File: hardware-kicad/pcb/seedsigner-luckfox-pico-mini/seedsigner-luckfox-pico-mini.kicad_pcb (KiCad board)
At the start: 2 copper layers, 100 x 100 mm, 37 parts, among them J1 Conn_01x10, J2 Conn_01x05, U1 LuckFox_Pico_PLUS_PRO, U2 RASPBERRY_PI_3_MODEL_B+

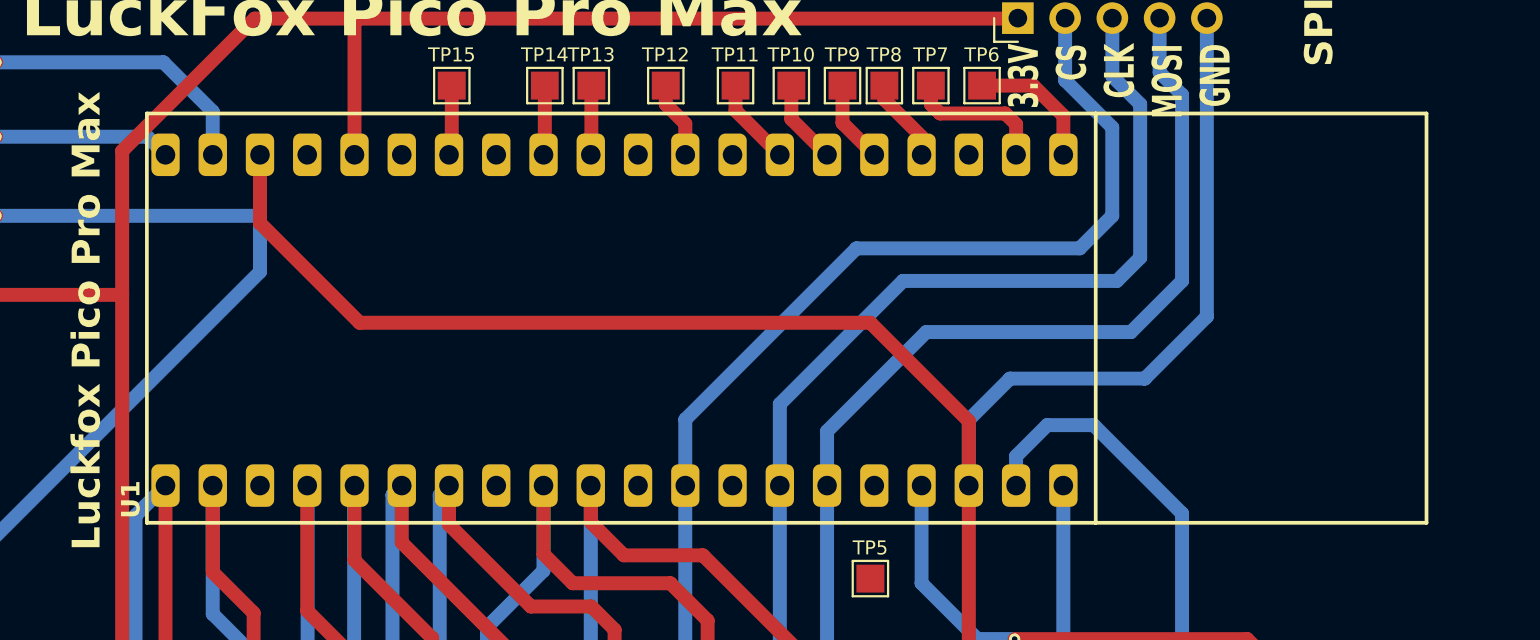
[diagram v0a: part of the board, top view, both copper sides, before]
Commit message: restructure dir structure and start luckfox-pico-mini pcb
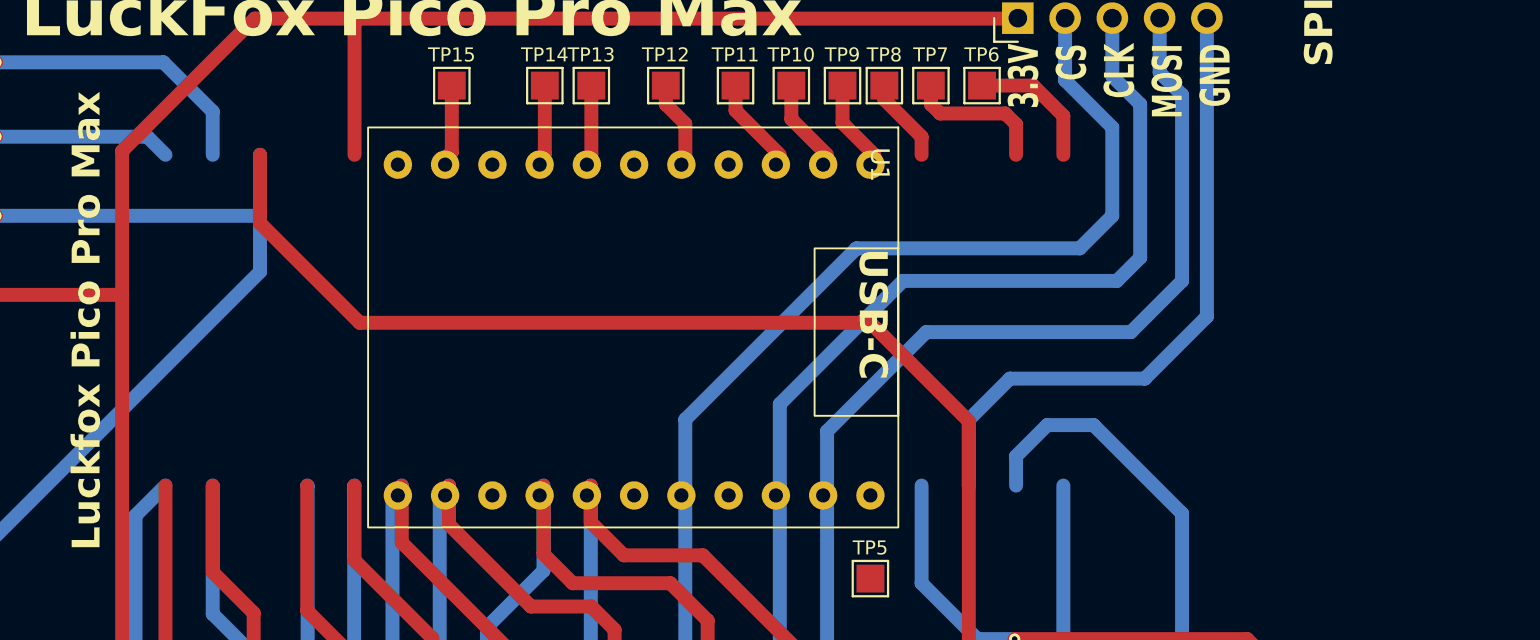
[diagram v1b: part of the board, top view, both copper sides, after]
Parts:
- U1: value LuckFox_Pico_PLUS_PRO -> LuckFox_Pico_MINI; footprint seedsigner-luckfox:LUCKFOX_PICO_PRO_MAX_PTH -> luckfox:LUCKFOX_PICO_MINI
- moved U1 41.6 mm to (55.8, 19.2), turned to -90 degrees
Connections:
- TP1 pad 1: Net-(U1-VBUS) -> unconnected-(TP1-Pad1)
- TP10 pad 1: Net-(U1-GPIO2_A2_d) -> unconnected-(TP10-Pad1)
- TP11 pad 1: Net-(U1-GPIO2_A3_d) -> unconnected-(TP11-Pad1)
- TP12 pad 1: Net-(U1-GPIO2_A6_d) -> unconnected-(TP12-Pad1)
- TP13 pad 1: Net-(U1-GPIO4_C0_z) -> unconnected-(TP13-Pad1)
- TP14 pad 1: Net-(U1-GPIO4_C1_z) -> unconnected-(TP14-Pad1)
- TP15 pad 1: Net-(U1-GPIO0_A7_d) -> unconnected-(TP15-Pad1)
- TP2 pad 1: Net-(U1-VSYS) -> unconnected-(TP2-Pad1)
- TP5 pad 1: Net-(U1-GPIO1_C3_d) -> unconnected-(TP5-Pad1)
- TP6 pad 1: Net-(U1-GPIO2_A4_d) -> unconnected-(TP6-Pad1)
- TP7 pad 1: Net-(U1-GPIO2_A5_d) -> unconnected-(TP7-Pad1)
- TP8 pad 1: Net-(U1-GPIO2_D0_d) -> unconnected-(TP8-Pad1)
- TP9 pad 1: Net-(U1-GPIO2_A1_d) -> unconnected-(TP9-Pad1)
- U1 pad 1: /KEY3 -> unconnected-(U1-VBUS-Pad1)
- U1 pad 10: /JOYSTICK_LEFT -> /DC
- U1 pad 11: unconnected-(U1-GPIO2_B1_d-Pad11) -> /KEY3
- U1 pad 12: /SPI_CS -> /JOYSTICK_LEFT
- U1 pad 13: unconnected-(U1-GND-Pad13) -> /JOYSTICK_UP
- U1 pad 14: /SPI_SCLK -> /JOYSTICK_PRESS
- U1 pad 15: /SPI_MOSI -> /JOYSTICK_DOWN
- U1 pad 16: Net-(U1-GPIO1_C3_d) -> /JOYSTICK_RIGHT
- U1 pad 17: /BACKLIGHT_PWM -> /KEY1
- U1 pad 18: GND -> /KEY2
- U1 pad 19: /DC -> unconnected-(U1-GPIO4_C0_z-Pad19)
- U1 pad 2: /KEY2 -> GND
- U1 pad 20: /RST -> unconnected-(U1-GPIO4_C1_z-Pad20)
- U1 pad 21: Net-(U1-GPIO2_A4_d) -> GND
- U1 pad 22: Net-(U1-GPIO2_A5_d) -> unconnected-(U1-1V8(OUT)-Pad22)
- U1 pad 3: unconnected-(U1-GND-Pad3) -> +3.3V
- U1 pad 4: /KEY1 -> unconnected-(U1-GPIO1_B2_d-Pad4)
- U1 pad 5: /JOYSTICK_RIGHT -> /BACKLIGHT_PWM
- U1 pad 6: /JOYSTICK_DOWN -> /SPI_CS
- U1 pad 7: /JOYSTICK_PRESS -> /SPI_SCLK
- U1 pad 8: unconnected-(U1-GND-Pad8) -> /SPI_MOSI
- U1 pad 9: /JOYSTICK_UP -> /RST
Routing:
- net unconnected-(TP2-Pad1): track 0.00 -> 17.6 mm, vias 0 -> 1
- net Net-(U1-VSYS): track 17.6 -> 0.00 mm, vias 1 -> 0
- net unconnected-(TP1-Pad1): track 0.00 -> 12.0 mm, vias 0 -> 1
- net Net-(U1-VBUS): track 12.0 -> 0.00 mm, vias 1 -> 0
- net unconnected-(TP7-Pad1): track 0.00 -> 7.67 mm
- net Net-(U1-GPIO2_A5_d): track 7.67 -> 0.00 mm
- net unconnected-(TP6-Pad1): track 0.00 -> 7.14 mm
- net Net-(U1-GPIO2_A4_d): track 7.14 -> 0.00 mm
- net unconnected-(TP11-Pad1): track 0.00 -> 4.71 mm
- net Net-(U1-GPIO2_A3_d): track 4.71 -> 0.00 mm
- net unconnected-(TP8-Pad1): track 0.00 -> 4.55 mm
- net Net-(U1-GPIO2_D0_d): track 4.55 -> 0.00 mm
- net unconnected-(TP10-Pad1): track 0.00 -> 4.52 mm
- net Net-(U1-GPIO2_A2_d): track 4.52 -> 0.00 mm
- net unconnected-(TP9-Pad1): track 0.00 -> 4.43 mm
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
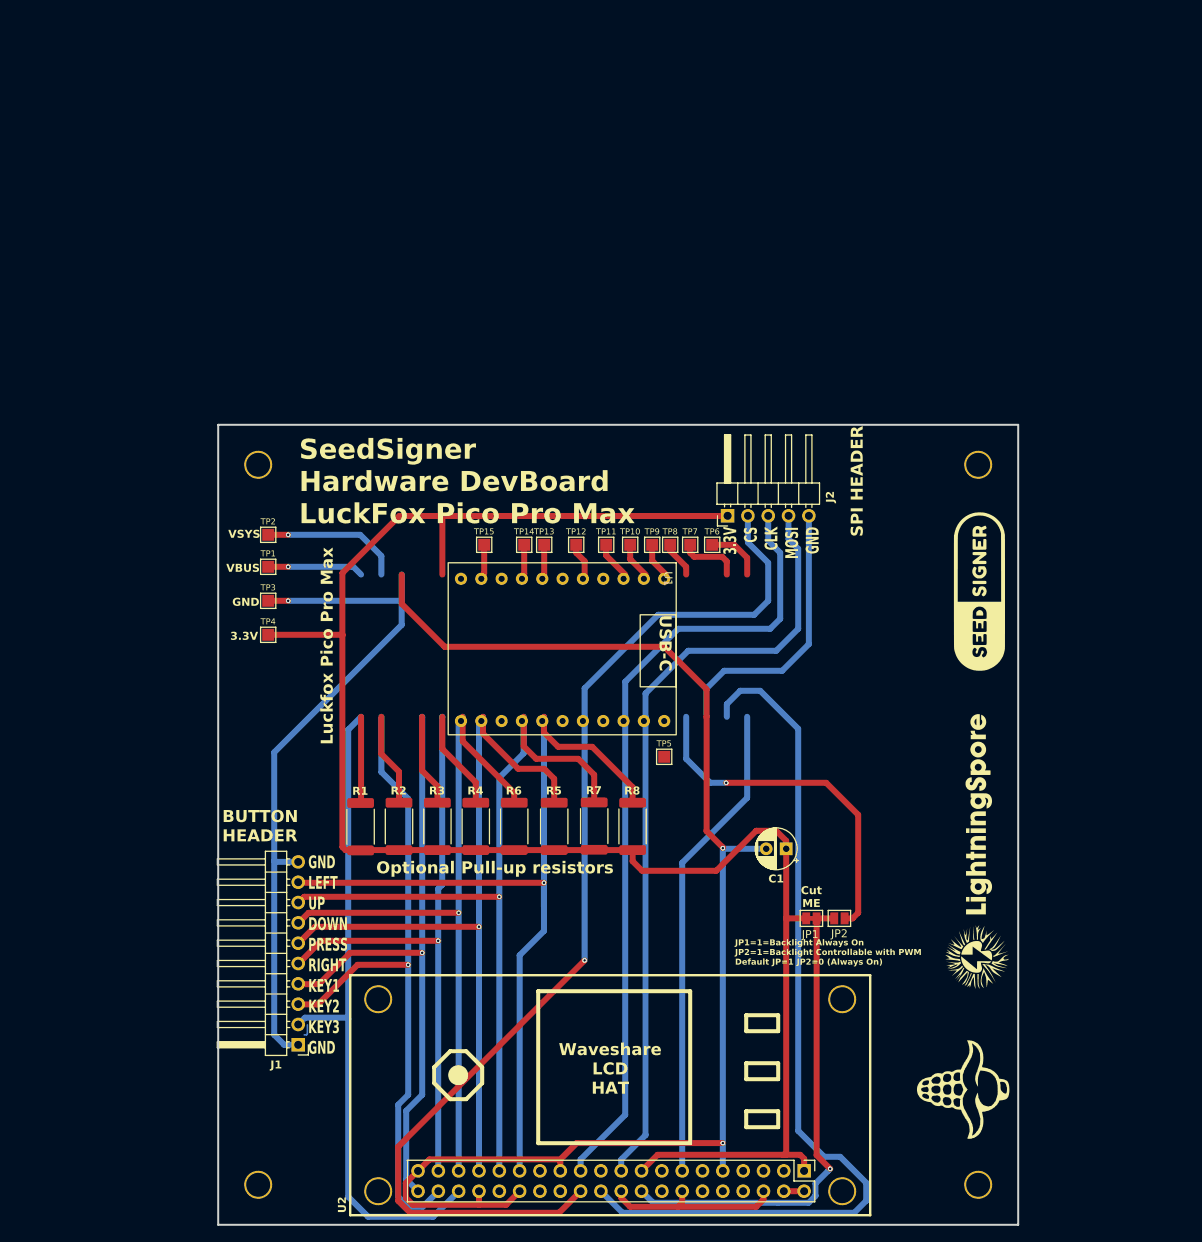
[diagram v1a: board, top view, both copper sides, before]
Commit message: add waveshare lcd 3d model and initial pcb routing
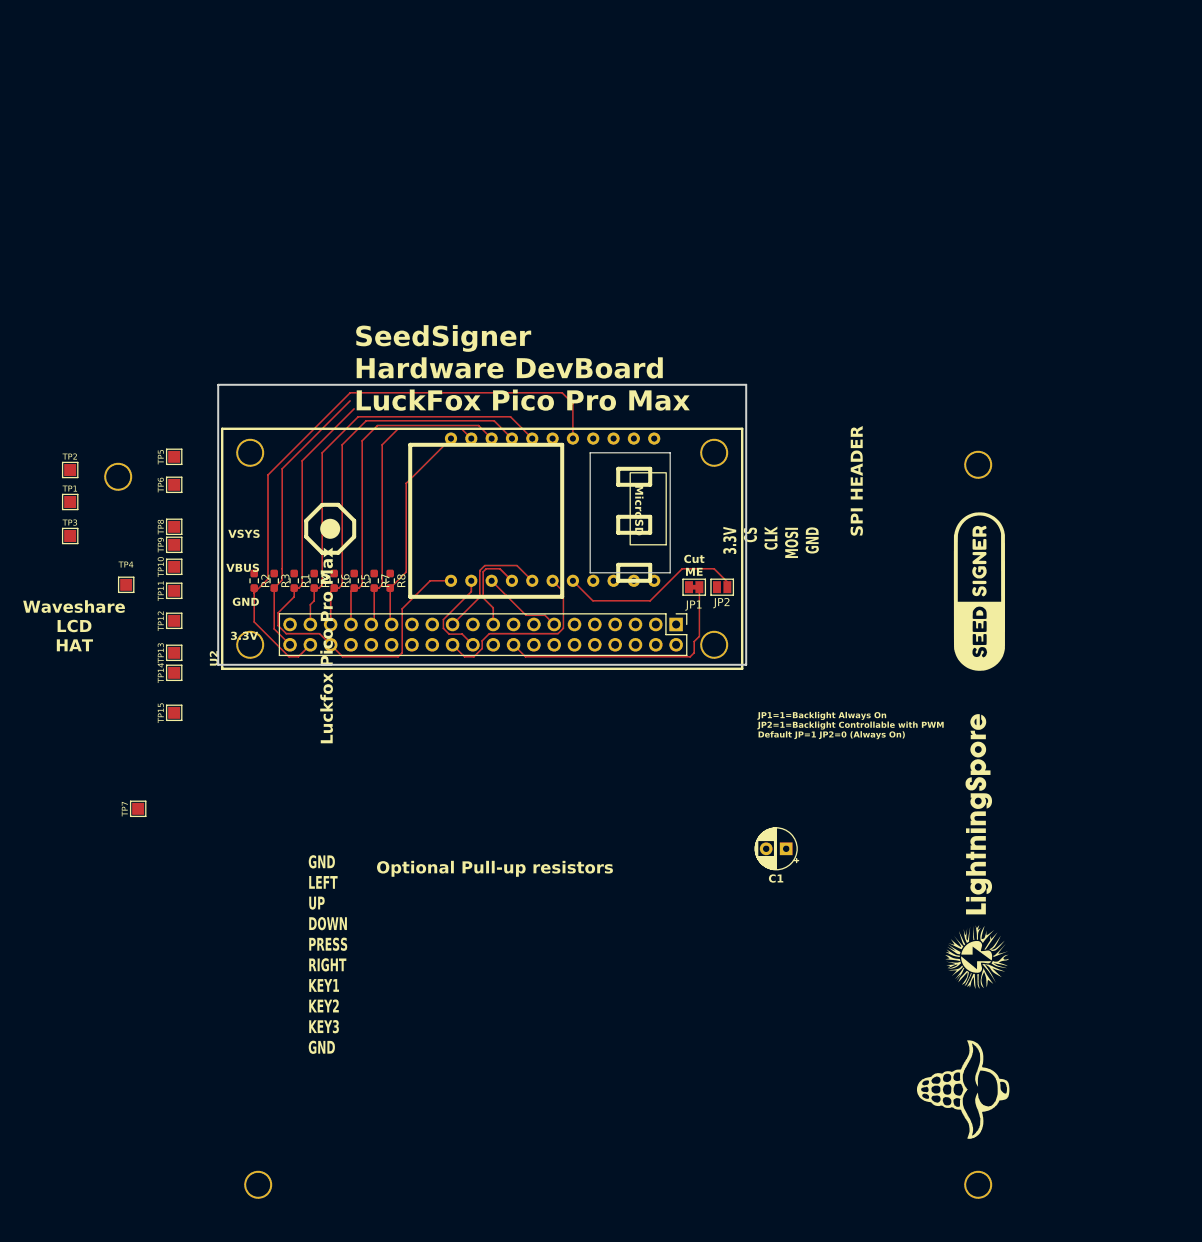
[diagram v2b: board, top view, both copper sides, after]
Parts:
- removed J1: Conn_01x10, seedsigner-luckfox:PinHeader_1x10_P2.54mm_Horizontal
- removed J2: Conn_01x05, seedsigner-luckfox:PinHeader_1x05_P2.54mm_Horizontal
- R1, R2, R3, R4, R5, R6, R7, R8: footprint seedsigner-luckfox:R_2512_6332Metric -> Resistor_SMD:R_0603_1608Metric_Pad0.98x0.95mm_HandSolder
- U1: moved to B.Cu
- moved TP7 2592.4 mm to (1632.6, -2045.2), turned to 90 degrees
- moved TP5 71.8 mm to (-5.50, 4.00), turned to 90 degrees
- moved U2 70.1 mm to (33.0, 15.5)
- moved TP6 67.7 mm to (-5.50, 7.50), turned to 90 degrees
- moved TP8 62.0 mm to (-5.50, 12.8), turned to 90 degrees
- moved TP9 59.8 mm to (-5.50, 15.0), turned to 90 degrees
- moved TP10 57.1 mm to (-5.50, 17.8), turned to 90 degrees
- moved TP11 54.3 mm to (-5.50, 20.8), turned to 90 degrees
- moved TP12 51.1 mm to (-5.50, 24.5), turned to 90 degrees
- moved TP13 48.2 mm to (-5.50, 28.5), turned to 90 degrees
- moved TP14 46.6 mm to (-5.50, 31.0), turned to 90 degrees
- moved TP15 44.1 mm to (-5.50, 36.0), turned to 90 degrees
- moved JP1 43.9 mm to (59.5, 20.3)
- moved JP2 43.9 mm to (63.0, 20.3)
- moved R8 43.1 mm to (21.5, 19.5), turned to -90 degrees
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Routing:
- net GND: track 319.4 -> 0.00 mm, vias 3 -> 0
- net +3.3V: track 226.9 -> 0.00 mm
- net /SPI_CS: track 137.5 -> 23.0 mm, vias 1 -> 0
- net /DC: track 111.8 -> 11.9 mm
- net /SPI_MOSI: track 98.0 -> 11.5 mm
- net /SPI_SCLK: track 99.6 -> 15.7 mm
- net /JOYSTICK_LEFT: track 109.6 -> 26.5 mm, vias 1 -> 0
- net /JOYSTICK_UP: track 100.9 -> 35.8 mm, vias 1 -> 0
- net /JOYSTICK_PRESS: track 96.8 -> 41.5 mm, vias 1 -> 0
- net /KEY1: track 89.4 -> 35.3 mm, vias 1 -> 0
- net /RST: track 60.1 -> 10.1 mm
- net /JOYSTICK_DOWN: track 91.0 -> 46.8 mm, vias 1 -> 0
- net /JOYSTICK_RIGHT: track 88.1 -> 51.7 mm, vias 1 -> 0
- net /KEY3: track 94.3 -> 61.8 mm
- net /BACKLIGHT: track 61.1 -> 31.9 mm, vias 1 -> 0
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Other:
- board size 100 x 100 mm -> 66 x 35 mm

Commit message: auto-route and cleanup of pico mini devboard
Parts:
- removed TP1, TP10, TP11, TP12, TP13, TP14, TP15, TP2, TP5, TP6, TP7, TP8, TP9: TestPoint, seedsigner-luckfox:TestPoint_Pad_1.5x1.5mm
- U1: moved to F.Cu
- moved TP3 89.2 mm to (70.2, 22.5)
- moved TP4 85.5 mm to (74.0, 22.5)
- moved LOGO1 85.3 mm to (10.8, 9.00), turned to 0 degrees
- moved ART1 81.6 mm to (18.0, 25.8), turned to 0 degrees
- moved LOGO2 74.4 mm to (72.6, 11.6), turned to 0 degrees
- moved C1 43.4 mm to (62.2, 10.5)
- moved H2 42.7 mm to (76.5, 56.5)
- moved H3 38.0 mm to (3.50, 57.0)
- moved U2 29.1 mm to (41.0, 43.5)
- moved U1 24.8 mm to (53.5, 3.50), turned to -90 degrees
- moved H4 18.1 mm to (77.0, 2.75)
- moved H1 15.9 mm to (3.00, 3.00)
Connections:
- JP1 pad 1: +3.3V -> /BACKLIGHT_PWM
- JP2 pad 1: /BACKLIGHT_PWM -> +3.3V
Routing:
- net +3.3V: track 0.00 -> 164.8 mm
- net GND: track 0.00 -> 138.1 mm
- net /SPI_CS: track 23.0 -> 83.5 mm, vias 0 -> 1
- net /RST: track 10.1 -> 61.4 mm, vias 0 -> 1
- net /DC: track 11.9 -> 55.8 mm
- net /SPI_MOSI: track 11.5 -> 52.2 mm
- net /SPI_SCLK: track 15.7 -> 55.3 mm, vias 0 -> 1
- net /KEY1: track 35.3 -> 69.5 mm, vias 0 -> 1
- net /BACKLIGHT: track 31.9 -> 50.5 mm, vias 0 -> 1
- net /JOYSTICK_LEFT: track 26.5 -> 44.3 mm
- net /BACKLIGHT_PWM: track 23.3 -> 39.1 mm, vias 0 -> 2
- net /JOYSTICK_RIGHT: track 51.7 -> 62.6 mm, vias 0 -> 1
- net /JOYSTICK_UP: track 35.8 -> 45.5 mm
- net /KEY3: track 61.8 -> 69.9 mm, vias 0 -> 1
- net /JOYSTICK_PRESS: track 41.5 -> 48.4 mm, vias 0 -> 1
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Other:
- board size 66 x 35 mm -> 80 x 60 mm
- board text added: "Luckfox Pico Mini Seedsigner Devboard"
- board text removed: "3.3V CS CLK MOSI GND"
- board text removed: "GND LEFT UP DOWN PRESS RIGHT KEY1 KEY2 KEY3 GND"
- board text removed: "JP1=1=Backlight Always On JP2=1=Backlight Controllable with PWM Default JP=1 JP2=0 (Always On)"
- board text removed: "Luckfox Pico Pro Max"
- board text removed: "Optional Pull-up resistors"
- board text removed: "SPI HEADER"
- board text removed: "VBUS"
- board text removed: "VSYS"
- board text removed: "Waveshare LCD HAT"

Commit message: finalize luckfox pico mini design
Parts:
- U1: footprint luckfox:LUCKFOX_PICO_MINI -> seedsigner-luckfox:LUCKFOX_PICO_MINI
- moved TP4 48.1 mm to (28.7, 6.30), turned to 90 degrees
- moved LOGO2 41.2 mm to (41.3, 38.4)
- moved TP3 35.7 mm to (38.5, 6.20), turned to 90 degrees
- moved C1 30.5 mm to (32.0, 6.30), turned to 0 degrees
- moved JP2 26.1 mm to (70.2, 45.4), turned to 90 degrees
- moved JP1 23.8 mm to (70.2, 41.6), turned to -90 degrees
- moved U1 18.8 mm to (71.9, 7.25)
- moved R6 15.4 mm to (29.9, 19.8)
- moved R3 15.4 mm to (22.4, 19.8)
- moved R2 15.4 mm to (19.9, 19.8)
- moved R8 13.5 mm to (35.0, 19.8)
- moved R7 12.9 mm to (32.4, 19.8)
- moved R4 12.9 mm to (24.9, 19.8)
- moved R5 10.4 mm to (27.4, 19.8)
- moved ART1 9.37 mm to (17.7, 16.4)
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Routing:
- net GND: track 138.1 -> 183.8 mm
- net /BACKLIGHT_PWM: track 39.1 -> 54.0 mm, vias 2 -> 0
- net /SPI_CS: track 83.5 -> 69.0 mm
- net /BACKLIGHT: track 50.5 -> 38.0 mm
- net /KEY1: track 69.5 -> 80.3 mm, vias 1 -> 2
- net /JOYSTICK_DOWN: track 53.7 -> 64.1 mm
- net /JOYSTICK_PRESS: track 48.4 -> 58.5 mm
- net /SPI_SCLK: track 55.3 -> 64.2 mm
- net /RST: track 61.4 -> 52.6 mm
- net /KEY2: track 73.3 -> 80.7 mm
- net /JOYSTICK_UP: track 45.5 -> 52.4 mm, vias 0 -> 1
- net /JOYSTICK_RIGHT: track 62.6 -> 67.8 mm
- net +3.3V: track 164.8 -> 160.4 mm, vias 0 -> 2
- net /KEY3: track 69.9 -> 72.3 mm, vias 1 -> 2
- net /JOYSTICK_LEFT: track 44.3 -> 46.6 mm, vias 0 -> 1
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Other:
- board text removed: "BUTTON HEADER"
- board text removed: "SeedSigner Hardware DevBoard LuckFox Pico Pro Max"
